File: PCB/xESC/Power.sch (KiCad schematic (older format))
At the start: 25 parts, among them U2 TMC6100-LA, U3 LMV321

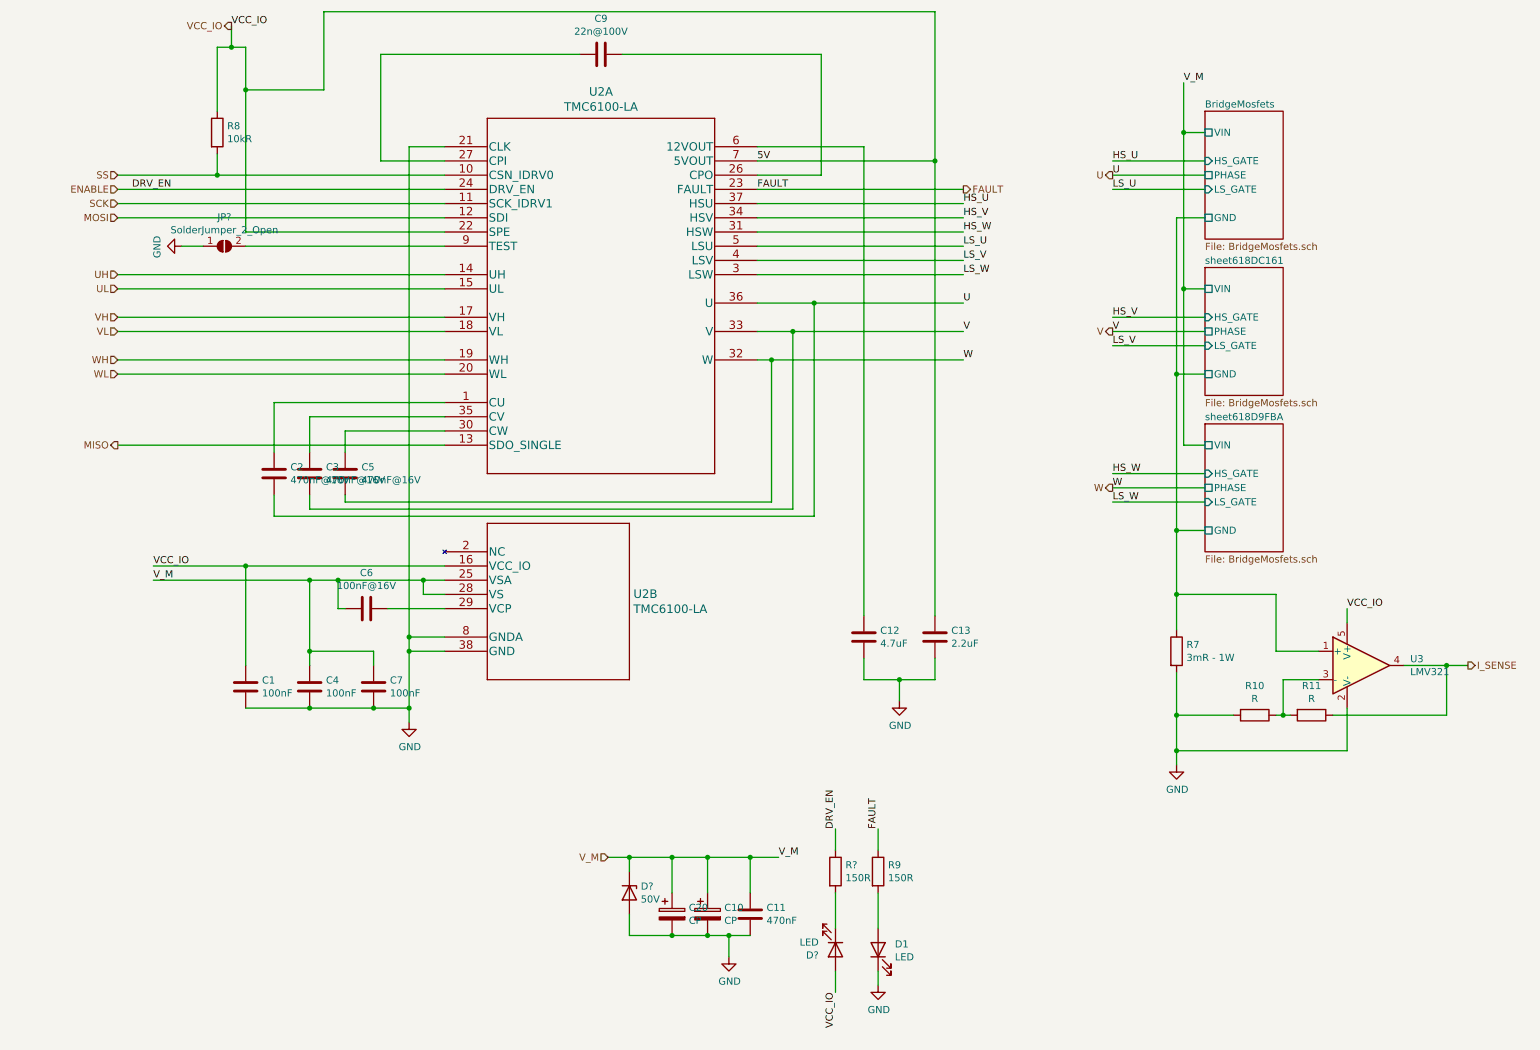
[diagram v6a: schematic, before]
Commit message: fixed silkscreen
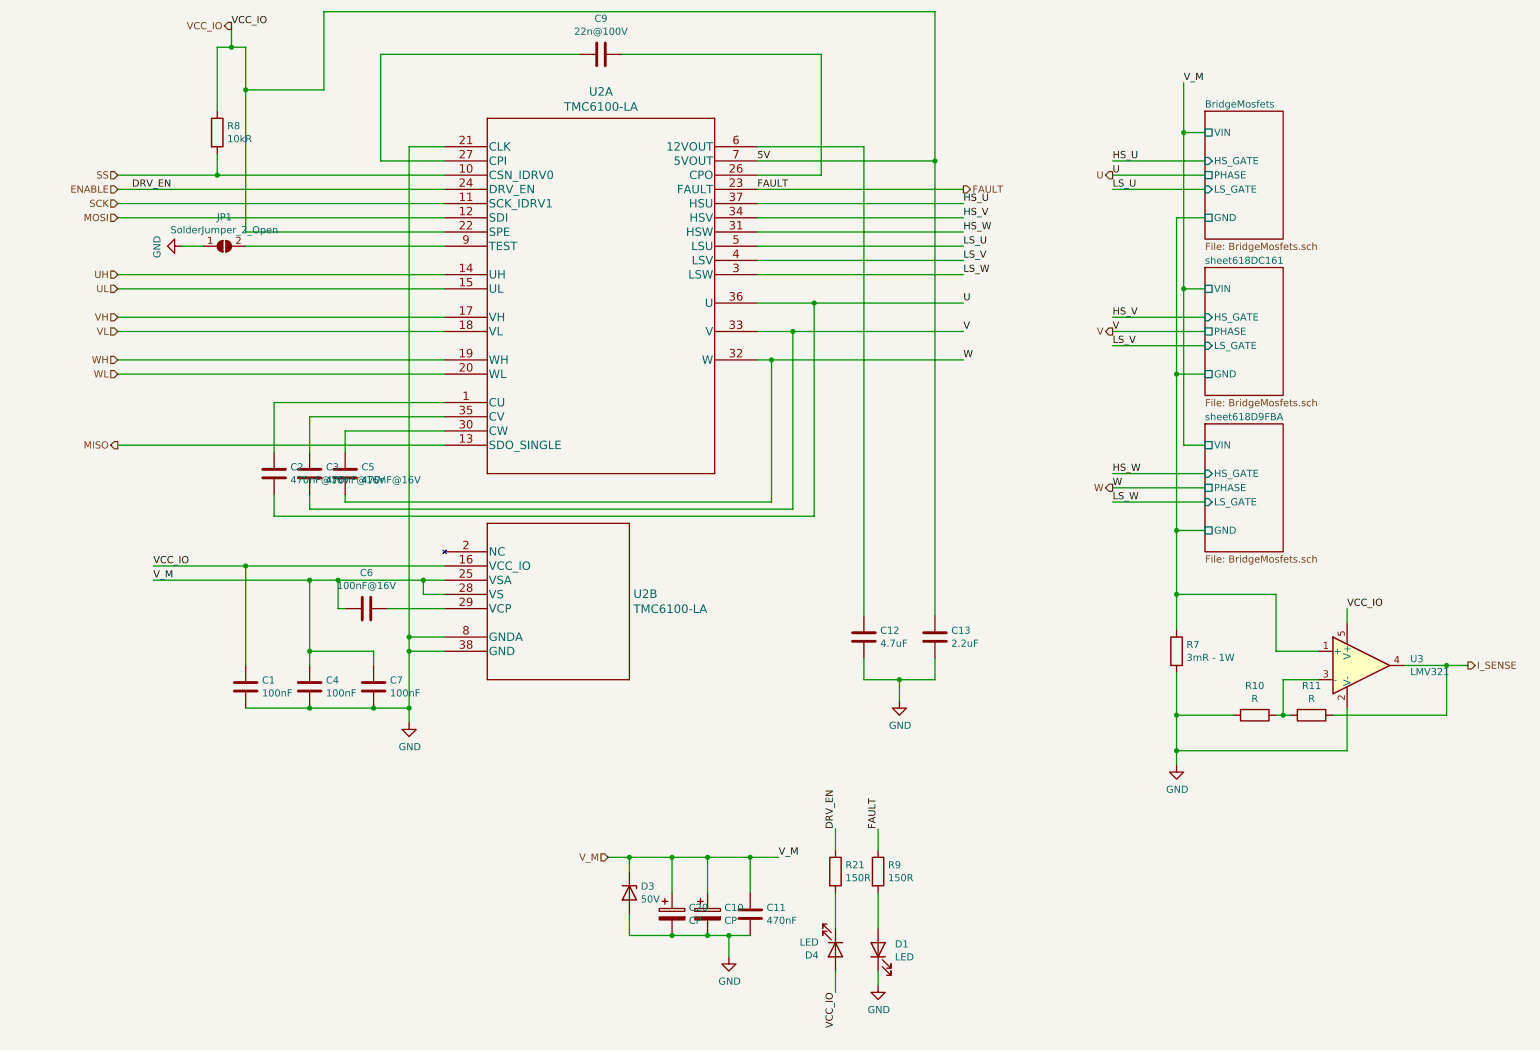
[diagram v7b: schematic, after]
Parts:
- D3: renamed from D?; footprint Diode_SMD:D_0805_2012Metric_Pad1.15x1.40mm_HandSolder -> Diode_SMD:D_SOT-23_ANK
- gave numbers to parts that had none: 3
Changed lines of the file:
@@
 VCC_IO
 $Comp
-L Device:R R?
+L Device:R R21
 U 1 1 6188DA17
 P 6350 6750
-F 0 "R?" H 6420 6796 50  0000 L CNN
+F 0 "R21" H 6420 6796 50  0000 L CNN
 F 1 "150R" H 6420 6705 50  0000 L CNN
 F 2 "Resistor_SMD:R_0805_2012Metric" V 6280 6750 50  0001 C CNN
@@
 $EndComp
 $Comp
-L Device:LED D?
+L Device:LED D4
 U 1 1 6188DA1D
 P 6350 7300
-F 0 "D?" V 6389 7182 50  0000 R CNN
+F 0 "D4" V 6389 7182 50  0000 R CNN
 F 1 "LED" V 6298 7182 50  0000 R CNN
 F 2 "LED_SMD:LED_0805_2012Metric_Pad1.15x1.40mm_HandSolder" H 6350 7300 50  0001 C CNN
@@
 	3600 2350 2200 2350
 $Comp
-L Jumper:SolderJumper_2_Open JP?
+L Jumper:SolderJumper_2_Open JP1
 U 1 1 618B45F2
 P 2050 2350
-F 0 "JP?" H 2050 2555 50  0000 C CNN
+F 0 "JP1" H 2050 2555 50  0000 C CNN
 F 1 "SolderJumper_2_Open" H 2050 2464 50  0000 C CNN
 F 2 "Jumper:SolderJumper-2_P1.3mm_Open_Pad1.0x1.5mm" H 2050 2350 50  0001 C CNN
@@
 	1900 2350 1750 2350
 $Comp
-L power:GND #PWR?
+L power:GND #PWR0114
 U 1 1 618B6034
 P 1750 2350
-F 0 "#PWR?" H 1750 2100 50  0001 C CNN
+F 0 "#PWR0114" H 1750 2100 50  0001 C CNN
 F 1 "GND" H 1755 2177 50  0000 C CNN
 F 2 "" H 1750 2350 50  0001 C CNN
@@
 Connection ~ 5200 6650
 $Comp
-L Device:D_Zener D?
+L Device:D_Zener D3
 U 1 1 618C9F81
 P 4900 6900
-F 0 "D?" V 4854 6980 50  0000 L CNN
+F 0 "D3" V 4854 6980 50  0000 L CNN
 F 1 "50V" V 4945 6980 50  0000 L CNN
-F 2 "Diode_SMD:D_0805_2012Metric_Pad1.15x1.40mm_HandSolder" H 4900 6900 50  0001 C CNN
+F 2 "Diode_SMD:D_SOT-23_ANK" H 4900 6900 50  0001 C CNN
 F 3 "~" H 4900 6900 50  0001 C CNN
 	1    4900 6900

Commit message: changed current sense amplifier to MCP601R, added values for current sense resistors
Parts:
- removed U3: LMV321, Package_TO_SOT_SMD:SOT-23-5_HandSoldering, symbol Amplifier_Operational:LMV321
- added U3: MCP601R, Package_TO_SOT_SMD:SOT-23-5_HandSoldering, symbol Amplifier_Operational:MCP601R
- R10: value R -> 1.5kR
- R11: value R -> 150kR
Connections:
- net BridgeMosfets/GND: now also U3.3 (+)
- net GND: now also U3.5 (V-)
- net I_SENSE: now also U3.1
- net VCC_IO: now also U3.2 (V+)
- net at R10.1, R11.2: now also U3.4 (-)
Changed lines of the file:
@@
 Wire Wire Line
 	2000 1850 3600 1850
-$Comp
-L Amplifier_Operational:LMV321 U3
-U 1 1 61A3792F
-P 10050 5300
-F 0 "U3" H 10394 5346 50  0000 L CNN
-F 1 "LMV321" H 10394 5255 50  0000 L CNN
-F 2 "Package_TO_SOT_SMD:SOT-23-5_HandSoldering" H 10050 5300 50  0001 L CNN
-F 3 "http://www.ti.com/lit/ds/symlink/lmv324.pdf" H 10050 5300 50  0001 C CNN
-	1    10050 5300
-	1    0    0    -1
-$EndComp
 Text Label 9950 4900 0    50   ~ 0
 VCC_IO
@@
 P 9300 5650
 F 0 "R10" V 9093 5650 50  0000 C CNN
-F 1 "R" V 9184 5650 50  0000 C CNN
+F 1 "1.5kR" V 9184 5650 50  0000 C CNN
 F 2 "Resistor_SMD:R_0805_2012Metric" V 9230 5650 50  0001 C CNN
 F 3 "~" H 9300 5650 50  0001 C CNN
@@
 P 9700 5650
 F 0 "R11" V 9493 5650 50  0000 C CNN
-F 1 "R" V 9584 5650 50  0000 C CNN
+F 1 "150kR" V 9584 5650 50  0000 C CNN
 F 2 "Resistor_SMD:R_0805_2012Metric" V 9630 5650 50  0001 C CNN
 F 3 "~" H 9700 5650 50  0001 C CNN
@@
 	4900 7200 5200 7200
 Connection ~ 5200 7200
+$Comp
+L Amplifier_Operational:MCP601R U3
+U 1 1 6188D007
+P 10050 5300
+F 0 "U3" H 10394 5346 50  0000 L CNN
+F 1 "MCP601R" H 10394 5255 50  0000 L CNN
+F 2 "Package_TO_SOT_SMD:SOT-23-5_HandSoldering" H 10050 5300 50  0001 C CNN
+F 3 "http://ww1.microchip.com/downloads/en/DeviceDoc/21314g.pdf" H 10050 5500 50  0001 C CNN
+	1    10050 5300
+	1    0    0    -1
+$EndComp
 $EndSCHEMATC
